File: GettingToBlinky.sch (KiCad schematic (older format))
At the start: 7 parts, among them U1 7555

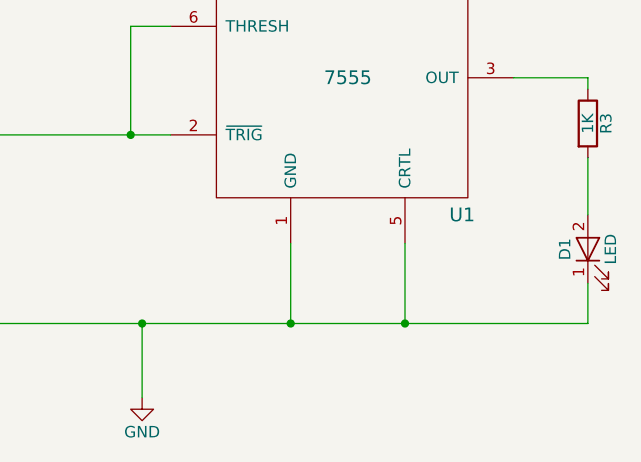
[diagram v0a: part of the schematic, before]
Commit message: fixed bug that ran a track from pin 5 to GND. also added laser cutter format, so we can generate stencil for applying solder paste
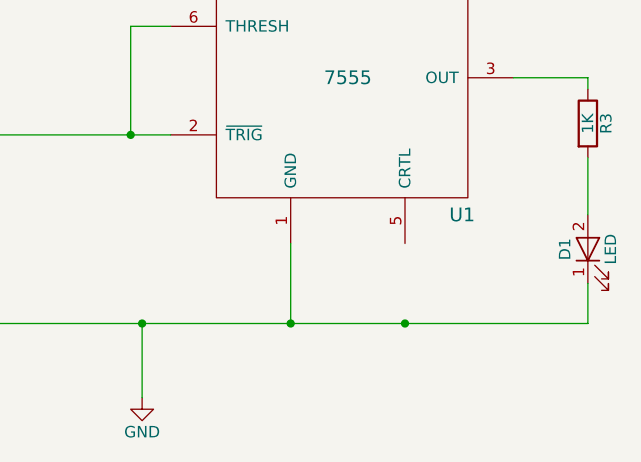
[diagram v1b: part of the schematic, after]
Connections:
- wire segments 22 -> 21
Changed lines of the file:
@@
 Text Label 3075 3175 0    60   ~ 0
 VDD
-Wire Wire Line
-	5900 4625 5900 4975
 Connection ~ 5900 4975
 $EndSCHEMATC
